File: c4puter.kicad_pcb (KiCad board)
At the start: 6 copper layers, 200 x 200 mm, 207 parts, among them J1 PDI, J2 MICROSD, J7 19V 3A, J8 DEBUG, Q1 AOD4189, Q2 AOD4189, Q3 2N7002, U1 ATXMEGA8E5-MU

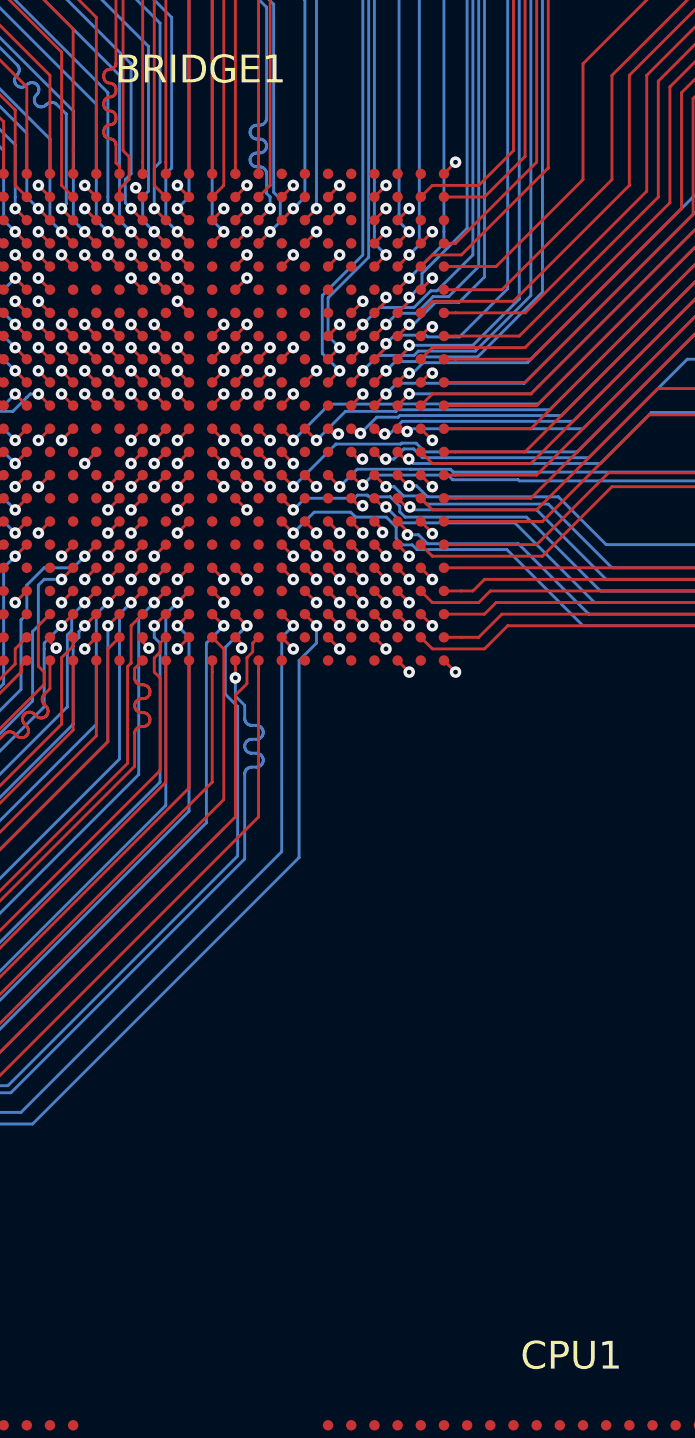
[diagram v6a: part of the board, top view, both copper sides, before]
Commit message: Break out CPU bus
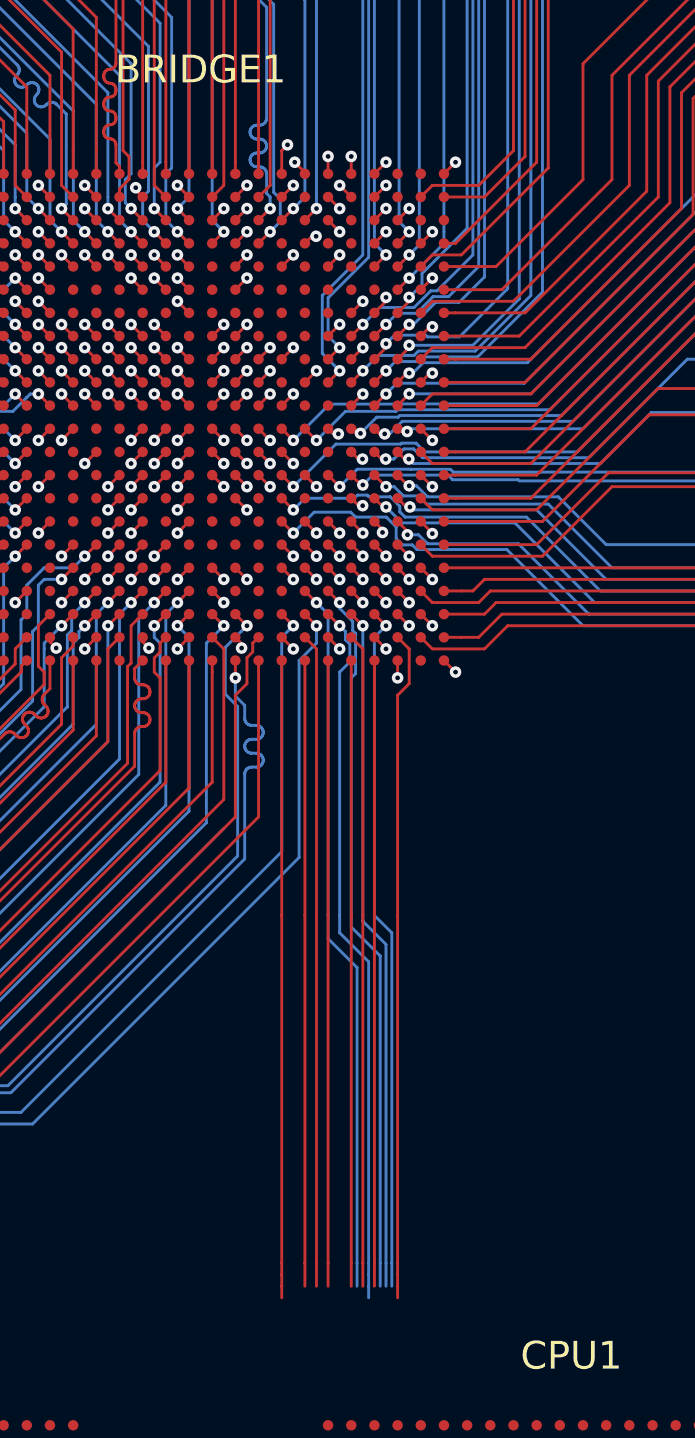
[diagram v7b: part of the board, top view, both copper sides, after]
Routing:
- net Net-(BRIDGE1-PadR22): track 0.00 -> 57.4 mm, vias 0 -> 1
- net Net-(BRIDGE1-PadU22): track 0.00 -> 56.6 mm, vias 0 -> 1
- net Net-(BRIDGE1-PadT22): track 0.00 -> 55.7 mm, vias 0 -> 1
- net Net-(BRIDGE1-PadV22): track 0.00 -> 55.2 mm, vias 0 -> 1
- net Net-(BRIDGE1-PadV21): track 0.00 -> 53.9 mm, vias 0 -> 1
- net Net-(BRIDGE1-PadW22): track 0.00 -> 53.7 mm, vias 0 -> 1
- net Net-(BRIDGE1-PadW20): track 0.71 -> 52.5 mm
- net Net-(BRIDGE1-PadG20): track 0.71 -> 52.4 mm
- net Net-(BRIDGE1-PadF18): track 0.71 -> 50.6 mm
- net Net-(BRIDGE1-PadU20): track 0.71 -> 50.4 mm
- net Net-(BRIDGE1-PadN20): track 0.71 -> 50.3 mm
- net Net-(BRIDGE1-PadC17): track 0.71 -> 49.7 mm
- net Net-(BRIDGE1-PadH18): track 0.71 -> 49.6 mm
- net Net-(BRIDGE1-PadT19): track 0.71 -> 49.1 mm
- net Net-(BRIDGE1-PadK18): track 0.71 -> 48.5 mm
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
